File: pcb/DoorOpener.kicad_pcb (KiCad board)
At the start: 2 copper layers, 92.6 x 72.6 mm, 22 parts, among them J1 Serial, J2 Serial, J3 14V, J4 Terminal, K1 FINDER-36.11, Q1 2N2219, SW1 POWER, SW2 Button, SW4 Button, SW5 Reset, U1 ESP-01v090, U2 ESP-01v090, U3 dcdc

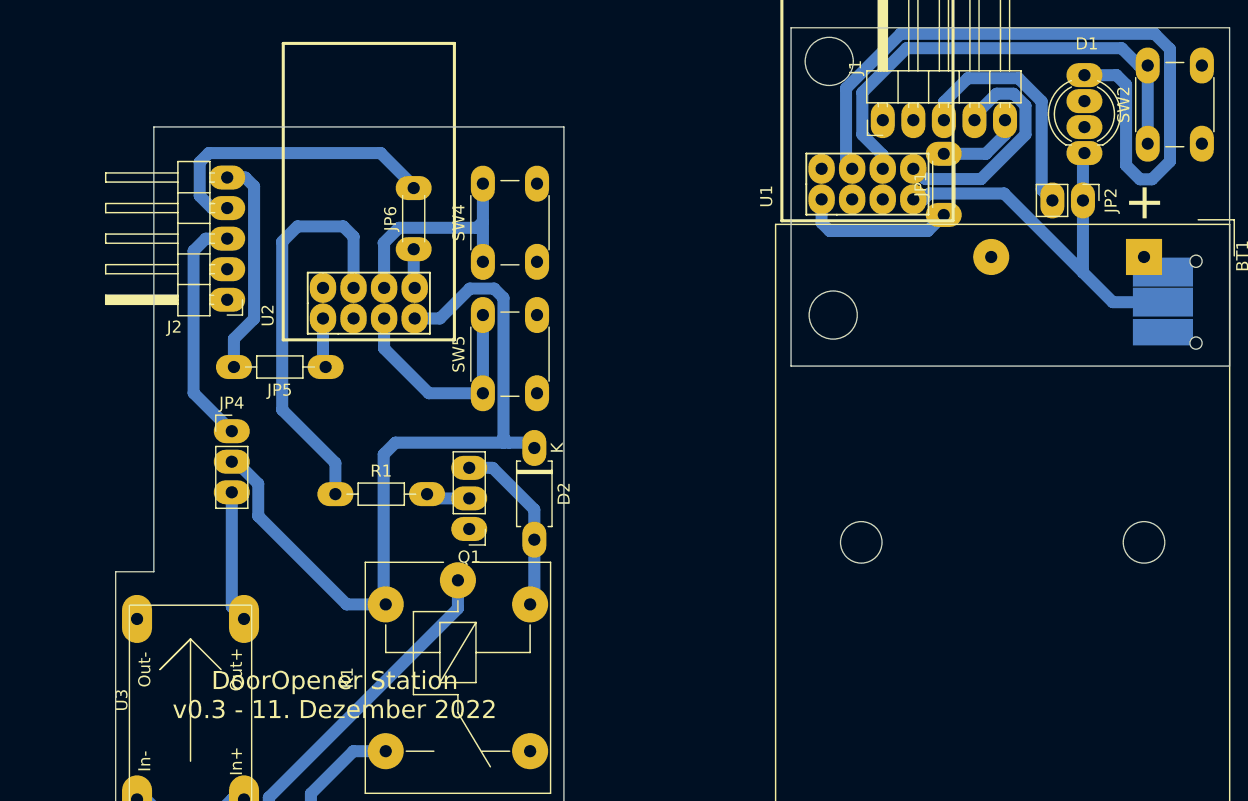
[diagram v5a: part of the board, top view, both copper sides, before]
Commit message: Add polarised capacitors for improved stability
Also add  a three way switch for the remote so that the jumper does not get lost and to decouple the battery when FTDI is used.
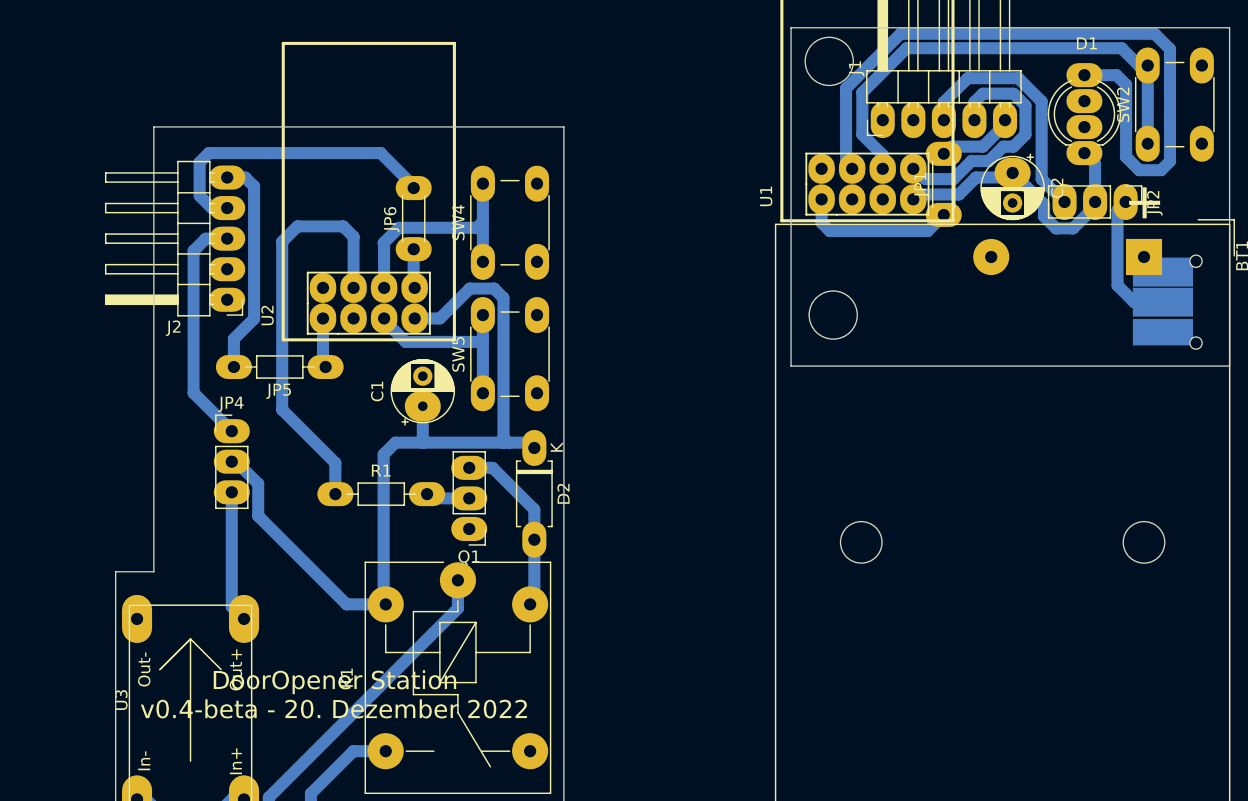
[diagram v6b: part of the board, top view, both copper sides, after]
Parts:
- added C1: C_Polarized, Capacitor_THT:CP_Radial_D5.0mm_P2.50mm, F.Cu at (126.0, 59.4)
- added C2: C_Polarized, Capacitor_THT:CP_Radial_D5.0mm_P2.50mm, F.Cu at (175.0, 40.0)
- J4: value Terminal -> 14V
- JP2: value FTDI_Voltage -> V_SWITCH; footprint Connector_PinHeader_2.54mm:PinHeader_1x02_P2.54mm_Vertical -> Connector_PinHeader_2.54mm:PinHeader_1x03_P2.54mm_Vertical
- Q1: value 2N2219 -> S9014
- R1: value R -> 1k
- moved JP2 3.55 mm to (184.4, 42.4)
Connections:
- J4 pad 1: (no net) -> Net-(J4-Pad1)
- J4 pad 2: (no net) -> Net-(J4-Pad2)
- JP2 pad 1: +3V3 -> Net-(SW1-Pad2)
- JP2 pad 2: Net-(J1-Pad3) -> +3V3
- K1 pad 11: Net-(K1-Pad11) -> Net-(J4-Pad1)
- K1 pad 14: Net-(K1-Pad14) -> Net-(J4-Pad2)
- SW1 pad 2: +3V3 -> Net-(SW1-Pad2)
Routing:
- net Net-(K1-Pad11): track 29.7 -> 0.00 mm
- net Net-(J4-Pad1): track 0.00 -> 29.7 mm
- net Net-(K1-Pad14): track 13.2 -> 0.00 mm
- net Net-(J4-Pad2): track 0.00 -> 13.2 mm
- net Net-(SW1-Pad2): track 0.00 -> 11.6 mm
- net +3V3: track 100.3 -> 92.8 mm
- net Net-(SW5-Pad1): track 18.7 -> 15.7 mm
- net Net-(D1-Pad4): track 60.8 -> 59.8 mm
- net /RX: track 23.9 -> 24.5 mm
- net Net-(J1-Pad3): track 19.8 -> 20.4 mm
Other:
- board text added: "DoorOpener Station v0.4-beta - 20. Dezember 2022"
- board text added: "v0.3-beta - 20.12.2022"
- board text removed: "DoorOpener Station v0.3 - 11. Dezember 2022"
- board text removed: "v0.2 - 3.12.2022"
